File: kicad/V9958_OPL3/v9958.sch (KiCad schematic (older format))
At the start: 20 parts, among them U1 74HCT139, U2 V9958, U3 DRAM_64KX4, U4 DRAM_64KX4, U5 DRAM_64KX4, U6 DRAM_64KX4, U8 YMF262, X2 OSC, Y1 21,443Mhz

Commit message: update
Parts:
- U8: footprint (none) -> Housings_SOIC:SOIC-24_7.5x15.4mm_Pitch1.27mm
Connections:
- net labels added: CLK, DOAB, SMPAC, SMPBD
- wire segments 173 -> 181
- no-connect marks 13 -> 14
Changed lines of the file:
@@
 /CS_VDP
 $Comp
-L VCC #PWR8
+L VCC #PWR01
 U 1 1 5A293DA5
 P 4550 3850
-F 0 "#PWR8" H 4550 3950 30  0001 C CNN
+F 0 "#PWR01" H 4550 3950 30  0001 C CNN
 F 1 "VCC" H 4550 3950 30  0000 C CNN
 F 2 "" H 4550 3850 60  0000 C CNN
@@
 $EndComp
 $Comp
-L GND-RESCUE-v9958 #PWR5
+L GND-RESCUE-v9958 #PWR02
 U 1 1 5A29423B
 P 4550 1200
-F 0 "#PWR5" H 4550 1200 30  0001 C CNN
+F 0 "#PWR02" H 4550 1200 30  0001 C CNN
 F 1 "GND" H 4550 1130 30  0001 C CNN
 F 2 "" H 4550 1200 60  0000 C CNN
@@
 $EndComp
 $Comp
-L GND-RESCUE-v9958 #PWR11
+L GND-RESCUE-v9958 #PWR03
 U 1 1 5A2957D7
 P 5100 900
-F 0 "#PWR11" H 5100 900 30  0001 C CNN
+F 0 "#PWR03" H 5100 900 30  0001 C CNN
 F 1 "GND" H 5100 830 30  0001 C CNN
 F 2 "" H 5100 900 60  0000 C CNN
@@
 $EndComp
 $Comp
-L GND-RESCUE-v9958 #PWR12
+L GND-RESCUE-v9958 #PWR04
 U 1 1 5A2958EA
 P 5700 900
-F 0 "#PWR12" H 5700 900 30  0001 C CNN
+F 0 "#PWR04" H 5700 900 30  0001 C CNN
 F 1 "GND" H 5700 830 30  0001 C CNN
 F 2 "" H 5700 900 60  0000 C CNN
@@
 $EndComp
 $Comp
-L GND-RESCUE-v9958 #PWR14
+L GND-RESCUE-v9958 #PWR05
 U 1 1 5A824C6E
 P 8250 1900
-F 0 "#PWR14" H 8250 1900 30  0001 C CNN
+F 0 "#PWR05" H 8250 1900 30  0001 C CNN
 F 1 "GND" H 8250 1830 30  0001 C CNN
 F 2 "" H 8250 1900 60  0000 C CNN
@@
 $EndComp
 $Comp
-L GND-RESCUE-v9958 #PWR16
+L GND-RESCUE-v9958 #PWR06
 U 1 1 5A825093
 P 10450 1950
-F 0 "#PWR16" H 10450 1950 30  0001 C CNN
+F 0 "#PWR06" H 10450 1950 30  0001 C CNN
 F 1 "GND" H 10450 1880 30  0001 C CNN
 F 2 "" H 10450 1950 60  0000 C CNN
@@
 $EndComp
 $Comp
-L GND-RESCUE-v9958 #PWR15
+L GND-RESCUE-v9958 #PWR07
 U 1 1 5A8252B2
 P 8300 3250
-F 0 "#PWR15" H 8300 3250 30  0001 C CNN
+F 0 "#PWR07" H 8300 3250 30  0001 C CNN
 F 1 "GND" H 8300 3180 30  0001 C CNN
 F 2 "" H 8300 3250 60  0000 C CNN
@@
 $EndComp
 $Comp
-L GND-RESCUE-v9958 #PWR17
+L GND-RESCUE-v9958 #PWR08
 U 1 1 5A8253E1
 P 10450 3300
-F 0 "#PWR17" H 10450 3300 30  0001 C CNN
+F 0 "#PWR08" H 10450 3300 30  0001 C CNN
 F 1 "GND" H 10450 3230 30  0001 C CNN
 F 2 "" H 10450 3300 60  0000 C CNN
@@
 D7
 $Comp
-L VCC #PWR13
+L VCC #PWR09
 U 1 1 5A8492E5
 P 6300 1050
-F 0 "#PWR13" H 6300 1150 30  0001 C CNN
+F 0 "#PWR09" H 6300 1150 30  0001 C CNN
 F 1 "VCC" H 6300 1150 30  0000 C CNN
 F 2 "" H 6300 1050 60  0000 C CNN
@@
 $EndComp
 $Comp
-L VCC #PWR1
+L VCC #PWR010
 U 1 1 5A849B3A
 P 800 650
-F 0 "#PWR1" H 800 750 30  0001 C CNN
+F 0 "#PWR010" H 800 750 30  0001 C CNN
 F 1 "VCC" H 800 750 30  0000 C CNN
 F 2 "" H 800 650 60  0000 C CNN
@@
 $EndComp
 $Comp
-L GND-RESCUE-v9958 #PWR2
+L GND-RESCUE-v9958 #PWR011
 U 1 1 5A849BF6
 P 800 1250
-F 0 "#PWR2" H 800 1250 30  0001 C CNN
+F 0 "#PWR011" H 800 1250 30  0001 C CNN
 F 1 "GND" H 800 1180 30  0001 C CNN
 F 2 "" H 800 1250 60  0000 C CNN
@@
 NoConn ~ 6200 1300
 $Comp
-L GND-RESCUE-v9958 #PWR6
+L GND-RESCUE-v9958 #PWR012
 U 1 1 5A860600
 P 4550 2000
-F 0 "#PWR6" H 4550 2000 30  0001 C CNN
+F 0 "#PWR012" H 4550 2000 30  0001 C CNN
 F 1 "GND" H 4550 1930 30  0001 C CNN
 F 2 "" H 4550 2000 60  0000 C CNN
@@
 $EndComp
 $Comp
-L VCC #PWR7
+L VCC #PWR013
 U 1 1 5A86085E
 P 4550 2100
-F 0 "#PWR7" H 4550 2200 30  0001 C CNN
+F 0 "#PWR013" H 4550 2200 30  0001 C CNN
 F 1 "VCC" H 4550 2200 30  0000 C CNN
 F 2 "" H 4550 2100 60  0000 C CNN
@@
 $EndComp
 $Comp
-L GND-RESCUE-v9958 #PWR3
+L GND-RESCUE-v9958 #PWR014
 U 1 1 5A93119E
 P 1100 2050
-F 0 "#PWR3" H 1100 2050 30  0001 C CNN
+F 0 "#PWR014" H 1100 2050 30  0001 C CNN
 F 1 "GND" H 1100 1980 30  0001 C CNN
 F 2 "" H 1100 2050 60  0000 C CNN
@@
 F 0 "U8" H 5350 6650 60  0000 C CNN
 F 1 "YMF262" H 5350 6550 60  0000 C CNN
-F 2 "" H 5350 6600 60  0000 C CNN
+F 2 "Housings_SOIC:SOIC-24_7.5x15.4mm_Pitch1.27mm" H 5350 6600 60  0001 C CNN
 F 3 "" H 5350 6600 60  0000 C CNN
 	1    5350 6600
@@
 /CS_IO0
 $Comp
-L GND-RESCUE-v9958 #PWR4
+L GND-RESCUE-v9958 #PWR015
 U 1 1 5B030726
 P 1300 6900
-F 0 "#PWR4" H 1300 6900 30  0001 C CNN
+F 0 "#PWR015" H 1300 6900 30  0001 C CNN
 F 1 "GND" H 1300 6830 30  0001 C CNN
 F 2 "" H 1300 6900 60  0000 C CNN
@@
 Text Label 4450 6400 0    60   ~ 0
 D7
+Text Label 4450 6550 0    60   ~ 0
+A0
+Text Label 4450 6650 0    60   ~ 0
+A1
+$Comp
+L OSC X2
+U 1 1 5B03C695
+P 5350 5200
+F 0 "X2" H 5350 5500 70  0000 C CNN
+F 1 "OSC" H 5350 5200 70  0000 C CNN
+F 2 "Oscillators:KXO-200_LargePads" H 5350 5200 60  0001 C CNN
+F 3 "" H 5350 5200 60  0000 C CNN
+	1    5350 5200
+	1    0    0    -1
+$EndComp
+NoConn ~ 6050 5350
+$Comp
+L VCC #PWR016
+U 1 1 5B03DBE3
+P 4600 4850
+F 0 "#PWR016" H 4600 4950 30  0001 C CNN
+F 1 "VCC" H 4600 4950 30  0000 C CNN
+F 2 "" H 4600 4850 60  0000 C CNN
+F 3 "" H 4600 4850 60  0000 C CNN
+	1    4600 4850
+	1    0    0    -1
+$EndComp
+$Comp
+L GND-RESCUE-v9958 #PWR017
+U 1 1 5B03DD31
+P 4600 5450
+F 0 "#PWR017" H 4600 5450 30  0001 C CNN
+F 1 "GND" H 4600 5380 30  0001 C CNN
+F 2 "" H 4600 5450 60  0000 C CNN
+F 3 "" H 4600 5450 60  0000 C CNN
+	1    4600 5450
+	1    0    0    -1
+$EndComp
+$Sheet
+S 9500 5650 1100 700
+U 5B03F723
+F0 "yac512" 60
+F1 "yac512.sch" 60
+F2 "DIN" I L 9500 5800 60
+F3 "CLK" I L 9500 5900 60
+F4 "SMP1" I L 9500 6000 60
+F5 "SMP2" I L 9500 6100 60
+$EndSheet
+$Comp
+L C C9
+U 1 1 5B040F41
+P 2800 900
+F 0 "C9" H 2825 1000 50  0000 L CNN
+F 1 "100n" H 2825 800 50  0000 L CNN
+F 2 "Capacitors_ThroughHole:C_Disc_D3_P2.5" H 2838 750 50  0001 C CNN
+F 3 "" H 2800 900 50  0001 C CNN
+	1    2800 900
+	1    0    0    -1
+$EndComp
+$Comp
+L C C10
+U 1 1 5B04100B
+P 3100 900
+F 0 "C10" H 3125 1000 50  0000 L CNN
+F 1 "100n" H 3125 800 50  0000 L CNN
+F 2 "Capacitors_ThroughHole:C_Disc_D3_P2.5" H 3138 750 50  0001 C CNN
+F 3 "" H 3100 900 50  0001 C CNN
+	1    3100 900
+	1    0    0    -1
+$EndComp
+Text GLabel 4500 7500 0    60   Input ~ 0
+/RESET
+Text GLabel 6350 7500 2    60   Input ~ 0
+/IRQ
 Wire Wire Line
 	4550 3850 4700 3850
@@
 Wire Wire Line
 	4550 6650 4300 6650
-Text Label 4450 6550 0    60   ~ 0
-A0
-Text Label 4450 6650 0    60   ~ 0
-A1
-$Comp
-L OSC X2
-U 1 1 5B03C695
-P 5350 5200
-F 0 "X2" H 5350 5500 70  0000 C CNN
-F 1 "OSC" H 5350 5200 70  0000 C CNN
-F 2 "Oscillators:KXO-200_LargePads" H 5350 5200 60  0001 C CNN
-F 3 "" H 5350 5200 60  0000 C CNN
-	1    5350 5200
-	1    0    0    -1
-$EndComp
 Wire Wire Line
 	6050 5050 6300 5050
@@
 Wire Wire Line
 	6300 5700 6150 5700
-NoConn ~ 6050 5350
-$Comp
-L VCC #PWR9
-U 1 1 5B03DBE3
-P 4600 4850
-F 0 "#PWR9" H 4600 4950 30  0001 C CNN
-F 1 "VCC" H 4600 4950 30  0000 C CNN
-F 2 "" H 4600 4850 60  0000 C CNN
-F 3 "" H 4600 4850 60  0000 C CNN
-	1    4600 4850
-	1    0    0    -1
-$EndComp
-$Comp
-L GND-RESCUE-v9958 #PWR10
-U 1 1 5B03DD31
-P 4600 5450
-F 0 "#PWR10" H 4600 5450 30  0001 C CNN
-F 1 "GND" H 4600 5380 30  0001 C CNN
-F 2 "" H 4600 5450 60  0000 C CNN
-F 3 "" H 4600 5450 60  0000 C CNN
-	1    4600 5450
-	1    0    0    -1
-$EndComp
 Wire Wire Line
 	4600 5450 4600 5350
@@
 Wire Wire Line
 	4600 5050 4650 5050
-$Sheet
-S 9500 5650 1100 700
-U 5B03F723
-F0 "yac512" 60
-F1 "yac512.sch" 60
-$EndSheet
-$Comp
-L C C9
-U 1 1 5B040F41
-P 2800 900
-F 0 "C9" H 2825 1000 50  0000 L CNN
-F 1 "100n" H 2825 800 50  0000 L CNN
-F 2 "Capacitors_ThroughHole:C_Disc_D3_P2.5" H 2838 750 50  0001 C CNN
-F 3 "" H 2800 900 50  0001 C CNN
-	1    2800 900
-	1    0    0    -1
-$EndComp
-$Comp
-L C C10
-U 1 1 5B04100B
-P 3100 900
-F 0 "C10" H 3125 1000 50  0000 L CNN
-F 1 "100n" H 3125 800 50  0000 L CNN
-F 2 "Capacitors_ThroughHole:C_Disc_D3_P2.5" H 3138 750 50  0001 C CNN
-F 3 "" H 3100 900 50  0001 C CNN
-	1    3100 900
-	1    0    0    -1
-$EndComp
 Connection ~ 2500 750
 Connection ~ 2800 750
@@
 	3100 1050 3100 1100
 Connection ~ 2800 1050
-Text GLabel 4500 7500 0    60   Input ~ 0
-/RESET
 Wire Wire Line
 	4500 7500 4550 7500
-Text GLabel 6350 7500 2    60   Input ~ 0
-/IRQ
 Wire Wire Line
 	6150 7500 6350 7500
+Wire Wire Line
+	6150 5800 6350 5800
+Wire Wire Line
+	6150 6000 6350 6000
+Wire Wire Line
+	6150 6100 6350 6100
+Wire Wire Line
+	6150 6200 6350 6200
+Wire Wire Line
+	9500 5800 9150 5800
+Wire Wire Line
+	9500 5900 9150 5900
+Wire Wire Line
+	9150 6000 9500 6000
+Wire Wire Line
+	9500 6100 9150 6100
+Text Label 6150 5800 0    60   ~ 0
+CLK
+Text Label 9150 5900 0    60   ~ 0
+CLK
+Text Label 6150 6000 0    60   ~ 0
+DOAB
+Text Label 9150 5800 0    60   ~ 0
+DOAB
+Text Label 6150 6100 0    60   ~ 0
+SMPAC
+Text Label 9150 6100 0    60   ~ 0
+SMPAC
+Text Label 6150 6200 0    60   ~ 0
+SMPBD
+Text Label 9150 6000 0    60   ~ 0
+SMPBD
+NoConn ~ 6150 5900
 $EndSCHEMATC

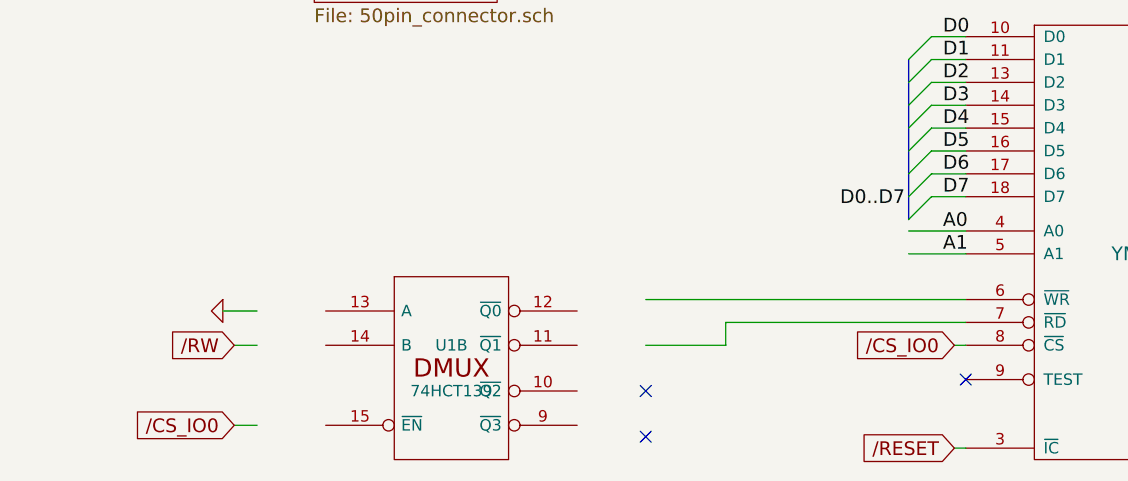
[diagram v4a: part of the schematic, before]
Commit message: generate OPL2 /CSW and /CSR by using PHI2 and RDY
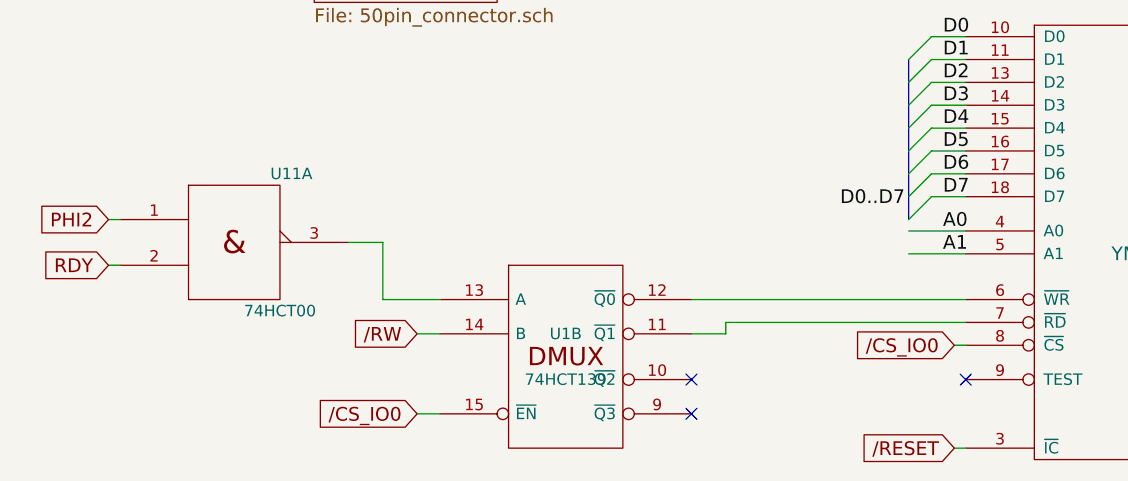
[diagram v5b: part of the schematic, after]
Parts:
- added U11: 74HCT00, Housings_DIP:DIP-14_W7.62mm_Socket_LongPads, symbol 7400
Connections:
- net labels added: PHI2
- wire segments 181 -> 185
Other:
- moved on the sheet: U1B
